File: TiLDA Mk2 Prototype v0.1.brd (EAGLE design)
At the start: 67.9 x 100 mm, 199 parts, among them IC1 ATSAM3X8EA-AU, IC10 MCP73831, IC2 MPU-6050, IC3 SRF-V1.2, IC5 S25FL216K0PMFI011, IC7 HMC5883LSMD (NP), IC8 MCP1825T-3302E/DC, IC9 TC1015-3V3, J1 ZX62-AB-5PA(11), J3 Arduino Headers, J5 1050270001 (NP), J6 B016 - PowerPOD NCP1402 5V0, J7 SFV30R-2STE1HLF, J8 1x02 RA Pin, Q10 2N7002KW, Q11 BSS84W, Q12 2N7002KW, Q13 BSS84W, Q8 BSS84W, Q9 2N7002KW, U2 JHD12864-G13BSW-OUTLINE, X1 12Mhz 13pF 30ppm (7pf caps), X2 32.768Khz

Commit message: Prototype: 0805 LED's
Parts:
- removed LOGO2: EMFLOGO-SYMBOL, TiLDA Mk2 Parts:EMFLOGO1
- RX, TX: device TiLDA Mk2 Parts:LED-0603-CORRECT -> TiLDA Mk2 Parts:LED-0805-CORRECT
- moved R48 4.76 mm to (55.2, 84.0)
- moved RX 1.00 mm to (18.2, 1.25)
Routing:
- net VBACKUP: track 312.4 -> 307.3 mm
- net BUTTON_CENTER: track 30.8 -> 33.8 mm
- net BUTTON_LEFT: track 28.1 -> 30.2 mm
- net RXL: track 81.9 -> 82.6 mm

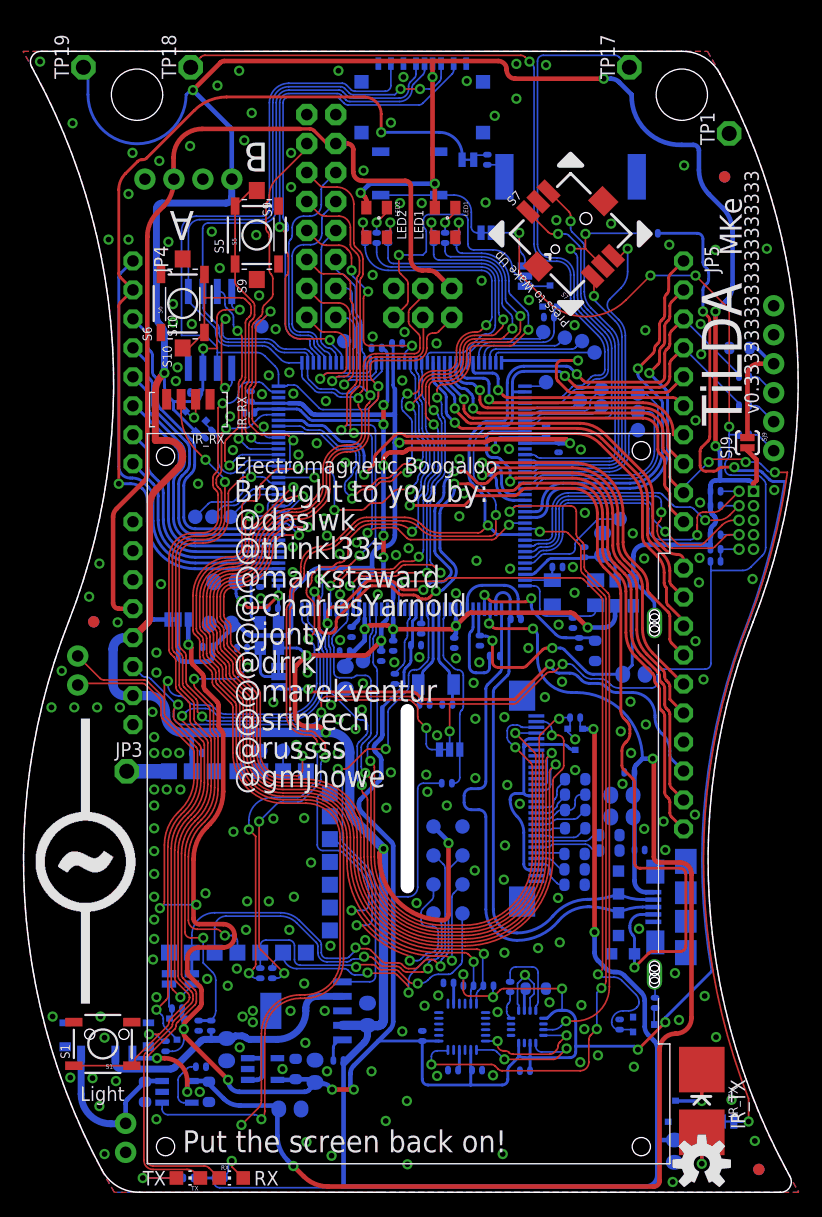
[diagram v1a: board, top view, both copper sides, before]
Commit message: Prototype: Minor tweaks, adding TP27, moved L102, L105
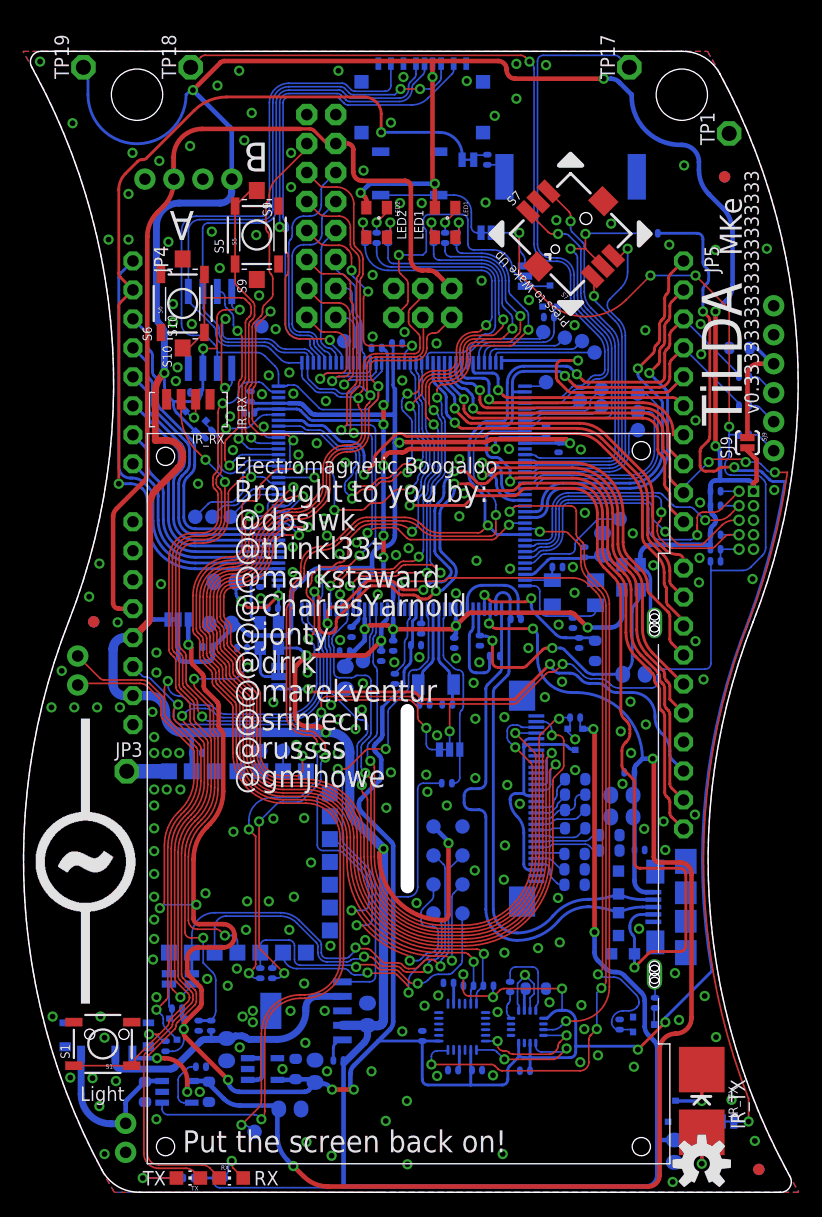
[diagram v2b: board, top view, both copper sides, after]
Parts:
- added TP27: PB10, TiLDA Mk2 Parts:B1,27
- moved L102 1.52 mm to (54.1, 53.9)
- moved L105 1.52 mm to (52.5, 53.9)
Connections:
- net LCD_CS renamed LCD_!CS
- net PB18 renamed A63
- net PB19 renamed A64
- net PC12 renamed D51
- net PC3 renamed D35
- net UOTGVBOF: now also TP27.TP
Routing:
- net 3V3: track 520.2 -> 517.7 mm
- net VDDOUT: track 87.3 -> 89.3 mm
- net VDDOUTIMI: track 25.0 -> 26.5 mm
- net UOTGVBOF: track 98.1 -> 99.5 mm
- net VDDPLL: track 10.3 -> 9.56 mm
- net MISO: track 160.6 -> 159.9 mm
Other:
- board text added: "27"
- board text added: "K"

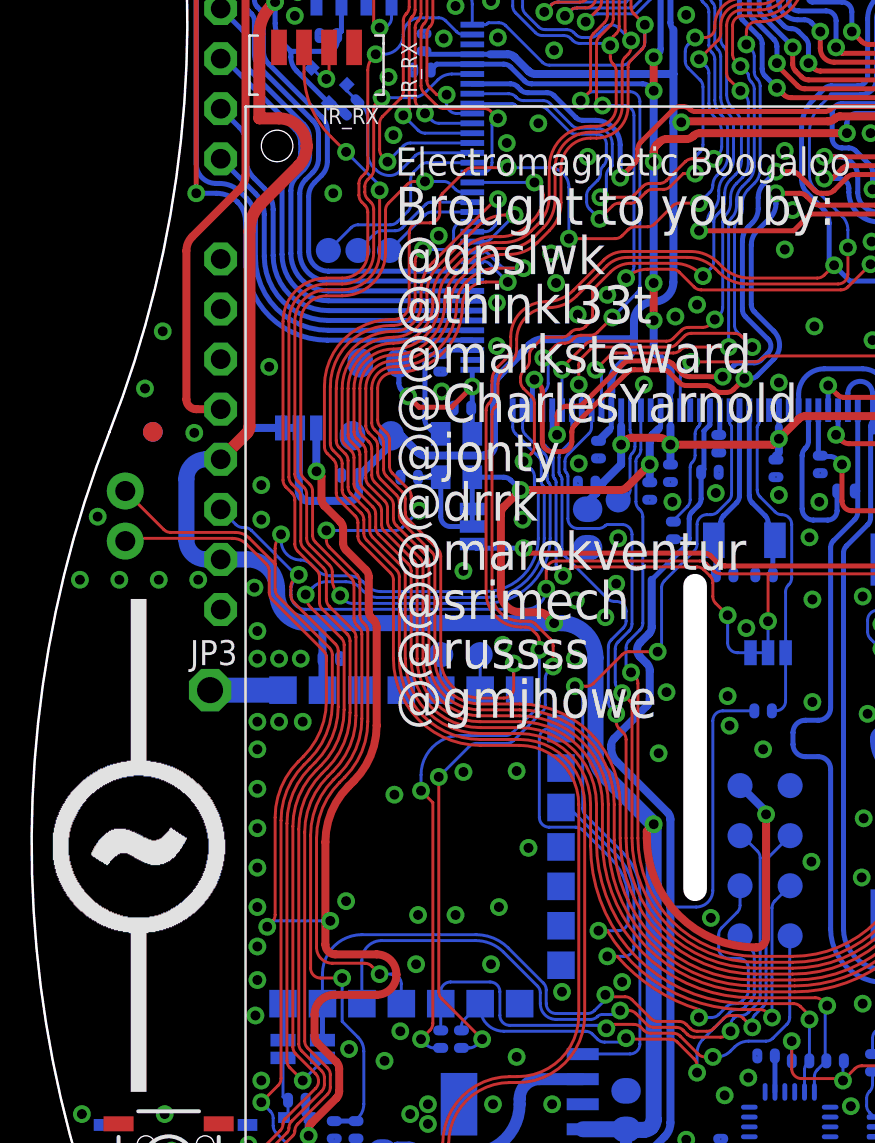
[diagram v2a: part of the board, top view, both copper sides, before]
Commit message: Prototype: Get backlight onto a PWM, swapped LCD_BACKLIGHT and TP25.
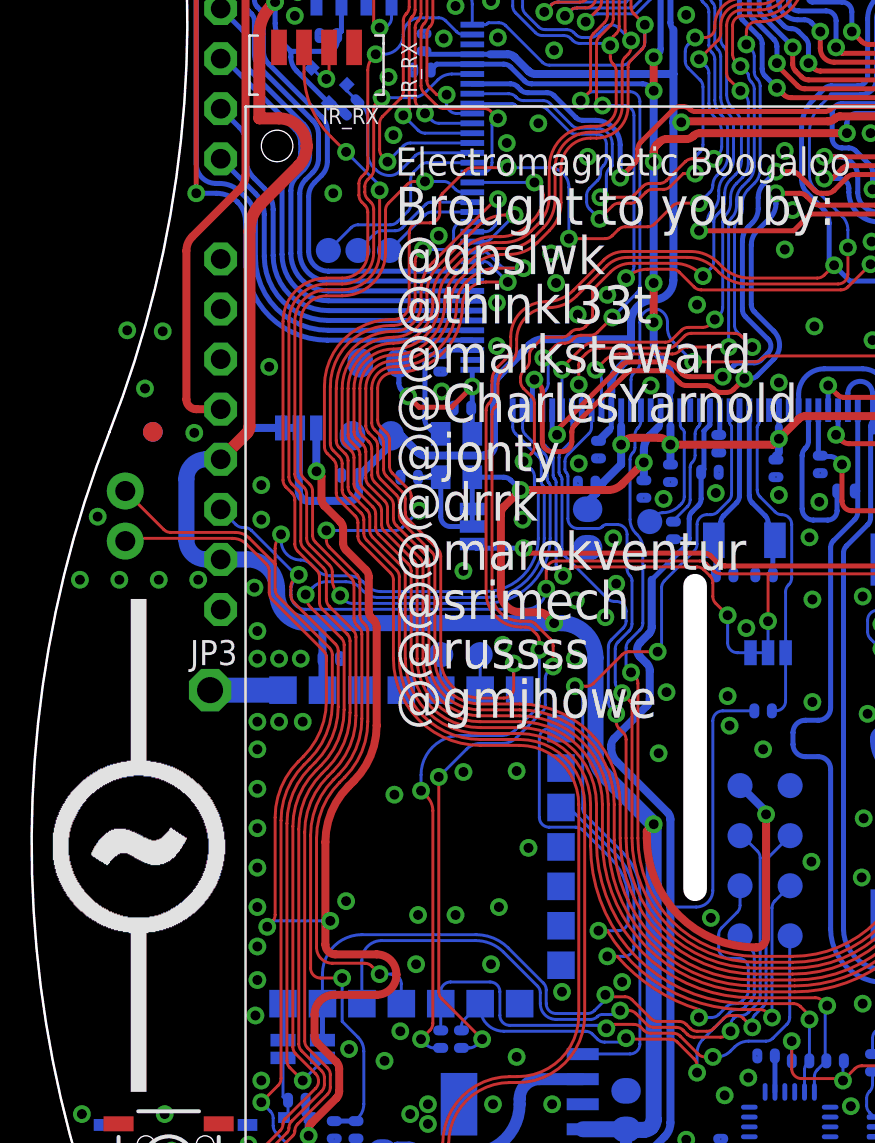
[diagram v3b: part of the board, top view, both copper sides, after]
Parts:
- TP25: value PC3 -> PC1
- moved TP25 1.94 mm to (31.4, 45.5)
- moved C106 0.32 mm to (31.1, 47.1)
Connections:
- removed net D35: IC1.60, TP25.TP
- new net D33: IC1.55, TP25.TP
- net LCD_BACKLIGHT: now also IC1.60; no longer IC1.55
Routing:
- net D33: track 0.00 -> 6.70 mm
- net LCD_BACKLIGHT: track 63.7 -> 69.9 mm
- net D35: track 4.98 -> 0.00 mm

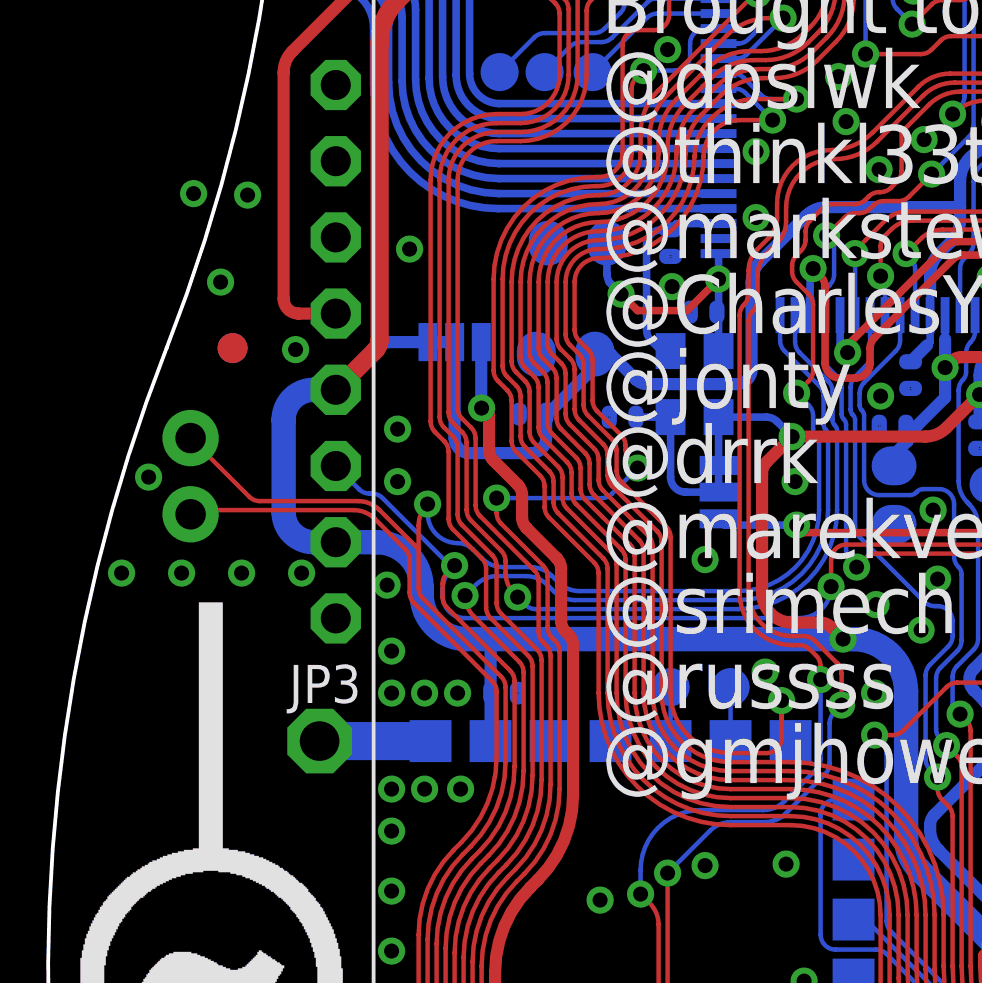
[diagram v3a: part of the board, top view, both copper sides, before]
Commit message: Prototype: Get LIGHT on to a wake up pin, swapped LIGTH with AT_COMMAND
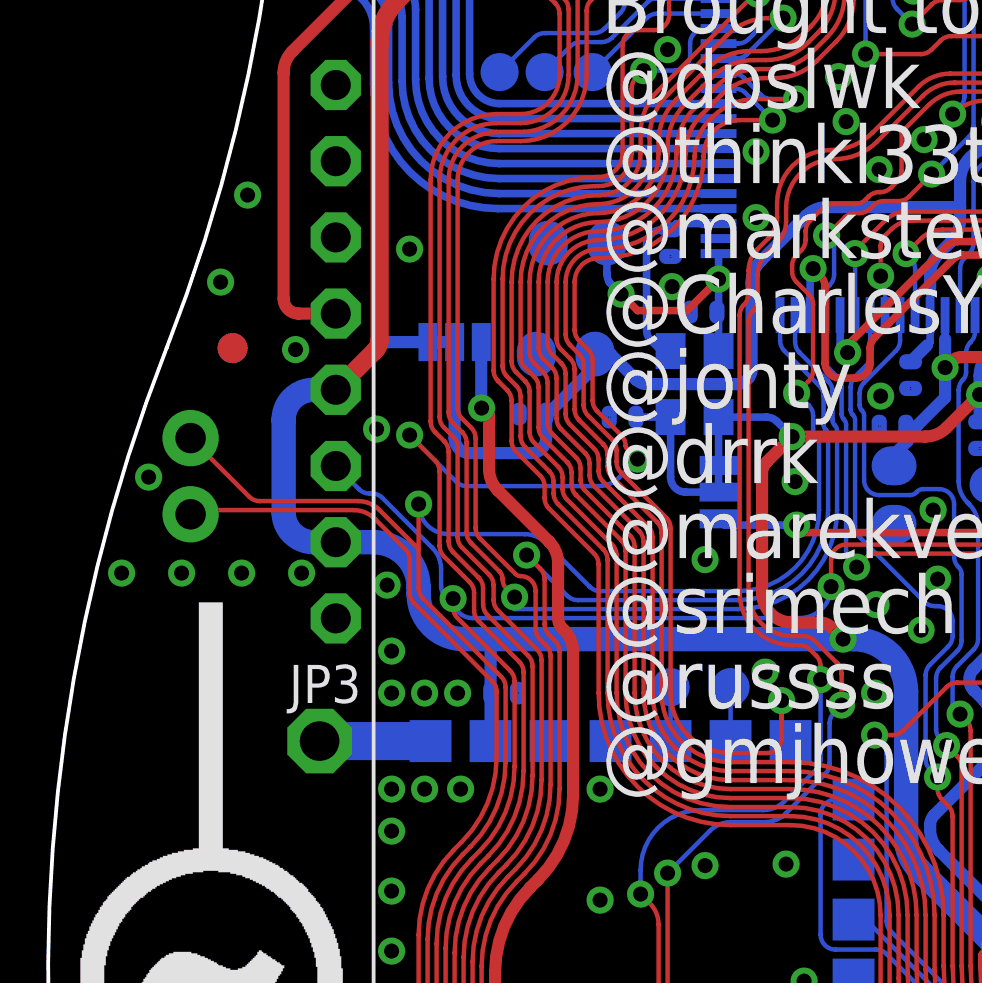
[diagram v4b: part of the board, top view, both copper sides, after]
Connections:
- net LIGHT: now also IC1.84; no longer IC1.72
- net SRF_P2_0/AT_COMMAND: now also IC1.72; no longer IC1.84
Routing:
- net LIGHT: track 63.0 -> 74.6 mm, vias 2 -> 4
- net SRF_P2_0/AT_COMMAND: track 51.7 -> 45.2 mm, vias 4 -> 2
- net MASTER_RESET: track 162.5 -> 160.6 mm
- net GND: vias 235 -> 234

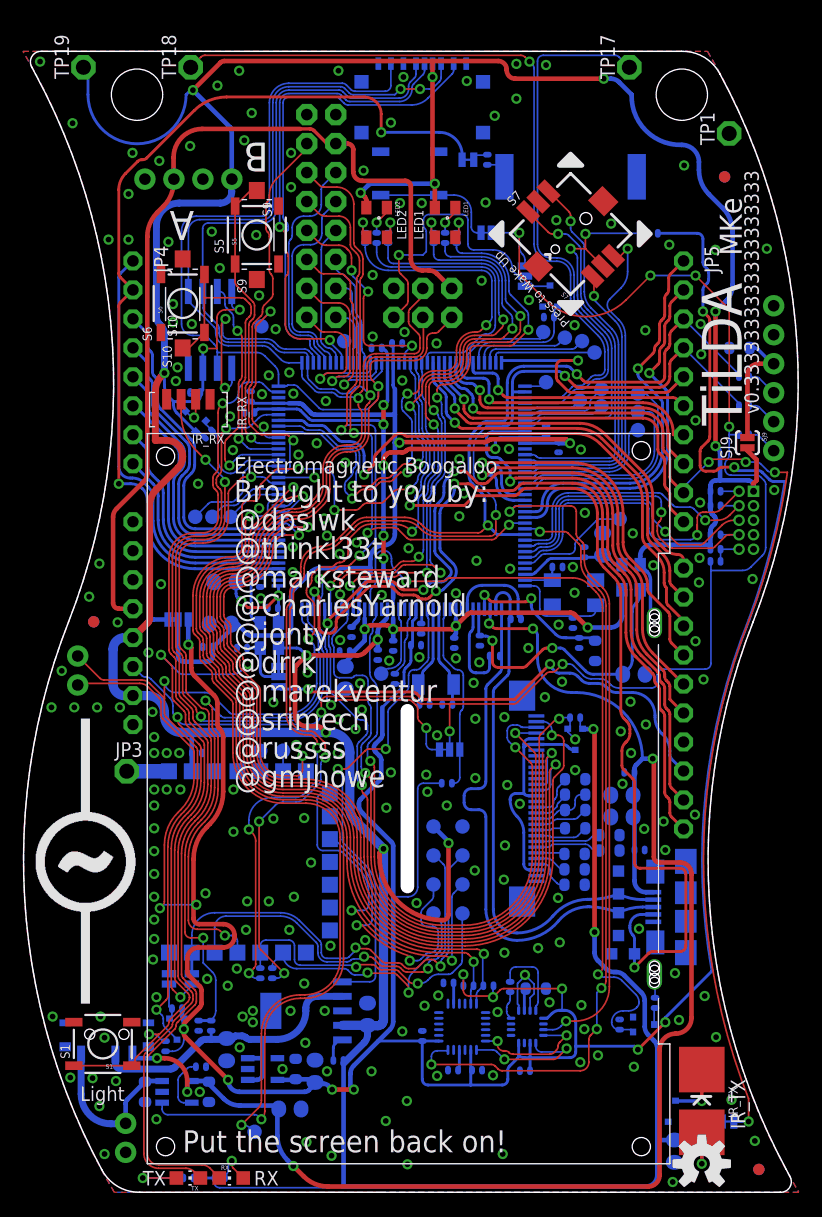
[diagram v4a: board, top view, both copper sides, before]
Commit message: Prototype: Artwork and trace tweak
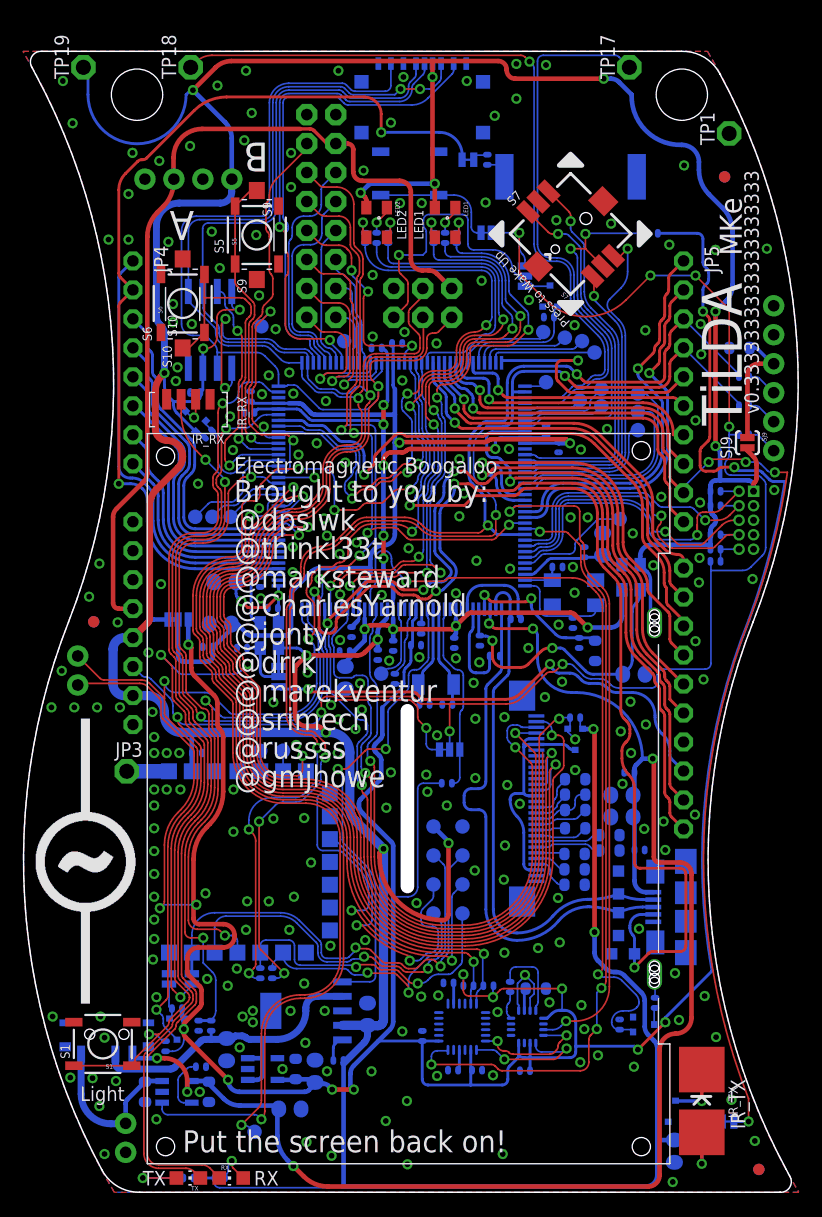
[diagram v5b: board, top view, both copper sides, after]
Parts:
- moved LOGO1 8.93 mm to (58.8, 11.4), flipped to the bottom
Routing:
- net 3V3: track 517.2 -> 515.8 mm
- net JTAG_TMS: track 29.4 -> 28.4 mm
- net JTAG_TDI: track 27.8 -> 27.1 mm
- net GND: vias 234 -> 237
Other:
- board text added: "Accel"
- board text added: "Compass"
- board text added: "Gyro"
- board text added: "µSD Socket"

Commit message: Prototype: VDDIO rewire
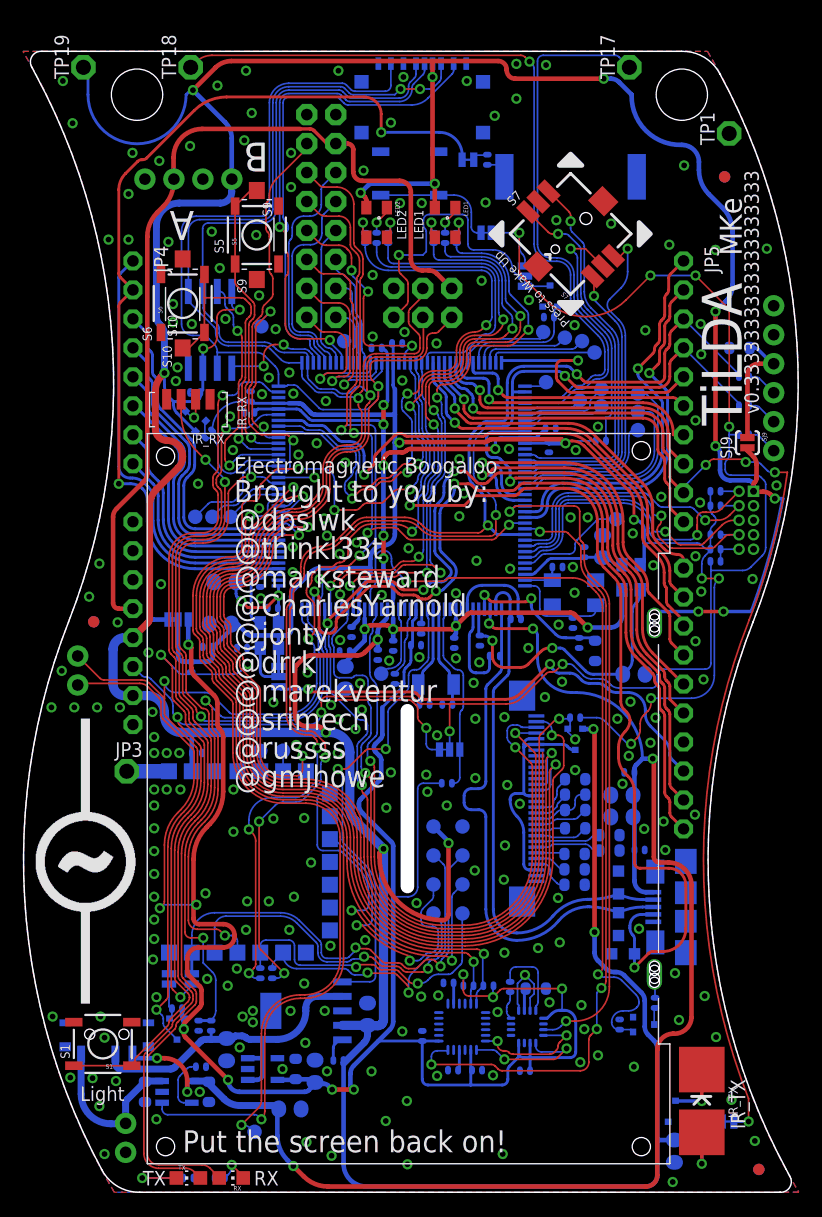
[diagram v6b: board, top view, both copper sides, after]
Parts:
- moved R47 33.3 mm to (14.8, 46.0), turned to 90 degrees
- moved R48 18.8 mm to (50.6, 65.8), turned to 0 degrees
- moved C105 0.85 mm to (46.1, 65.3)
- moved C113 0.45 mm to (46.2, 67.0), turned to 0 degrees
- moved TP26 0.30 mm to (52.0, 59.0)
- moved C133 0.20 mm to (50.8, 56.6)
- turned R49 to 315 degrees
- turned RX to 180 degrees
- turned TX to 0 degrees
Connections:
- removed net N$11: R8.1, TX.A
- removed net N$13: R14.1, RX.A
- new net N$2: R8.1, TX.C
- new net N$3: R14.1, RX.C
- new net VDDIO: C101.+, C104.2, C105.2, C107.2, C108.2, C118.2, IC1.105, IC1.11, IC1.125, IC1.62, L101.1, L102.1, R21.2, R22.2, R23.2, R24.2, R44.2, R47.2, R48.2, R49.1, SJ10.2, SJ8.3
- net 3V3: no longer C101.+, C104.2, C105.2, C107.2, C108.2, C118.2, IC1.105, IC1.11, IC1.125, IC1.62, L101.1, L102.1, R14.2, R21.2, R22.2, R23.2, R24.2, R44.2, R49.1, R8.2, SJ10.2, SJ8.3
- net GND: now also R14.2, R8.2
- net RXL: now also RX.A; no longer RX.C
- net TXL: now also TX.A; no longer TX.C
- net VBACKUP: no longer R47.2, R48.2
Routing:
- net VDDIO: track 0.00 -> 150.3 mm, vias 0 -> 7
- net 3V3: track 515.8 -> 410.4 mm
- net VBACKUP: track 307.2 -> 212.6 mm, vias 14 -> 10
- net FLASH_CS: track 18.9 -> 9.55 mm
- net N$2: track 0.00 -> 6.61 mm, vias 0 -> 1
- net N$11: track 6.51 -> 0.00 mm, vias 1 -> 0
- net BUTTON_CENTER: track 33.8 -> 29.1 mm, vias 2 -> 1
- net N$13: track 3.57 -> 0.00 mm, vias 1 -> 0
- net N$3: track 0.00 -> 2.90 mm, vias 0 -> 1
- net LIGHT: track 74.6 -> 72.3 mm, vias 4 -> 3
- net UOTGID: track 85.6 -> 83.9 mm
- net VBUS: track 130.7 -> 130.0 mm
- net GND: track 7.05 -> 7.15 mm, vias 237 -> 239
